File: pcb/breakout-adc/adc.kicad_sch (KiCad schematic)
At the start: 102 parts, among them J16 Conn_01x02_Pin, J17 Conn_01x02_Pin, J18 Conn_01x02_Pin, J19 Conn_01x02_Pin, U1 LMH6551MA, U2 LMH6551MA, U3 74AVC9112, U4 ADC10DL065, U5 74LS574, U6 74LS574, U7 74LS574, X1 SG-8101CE 50Mhz

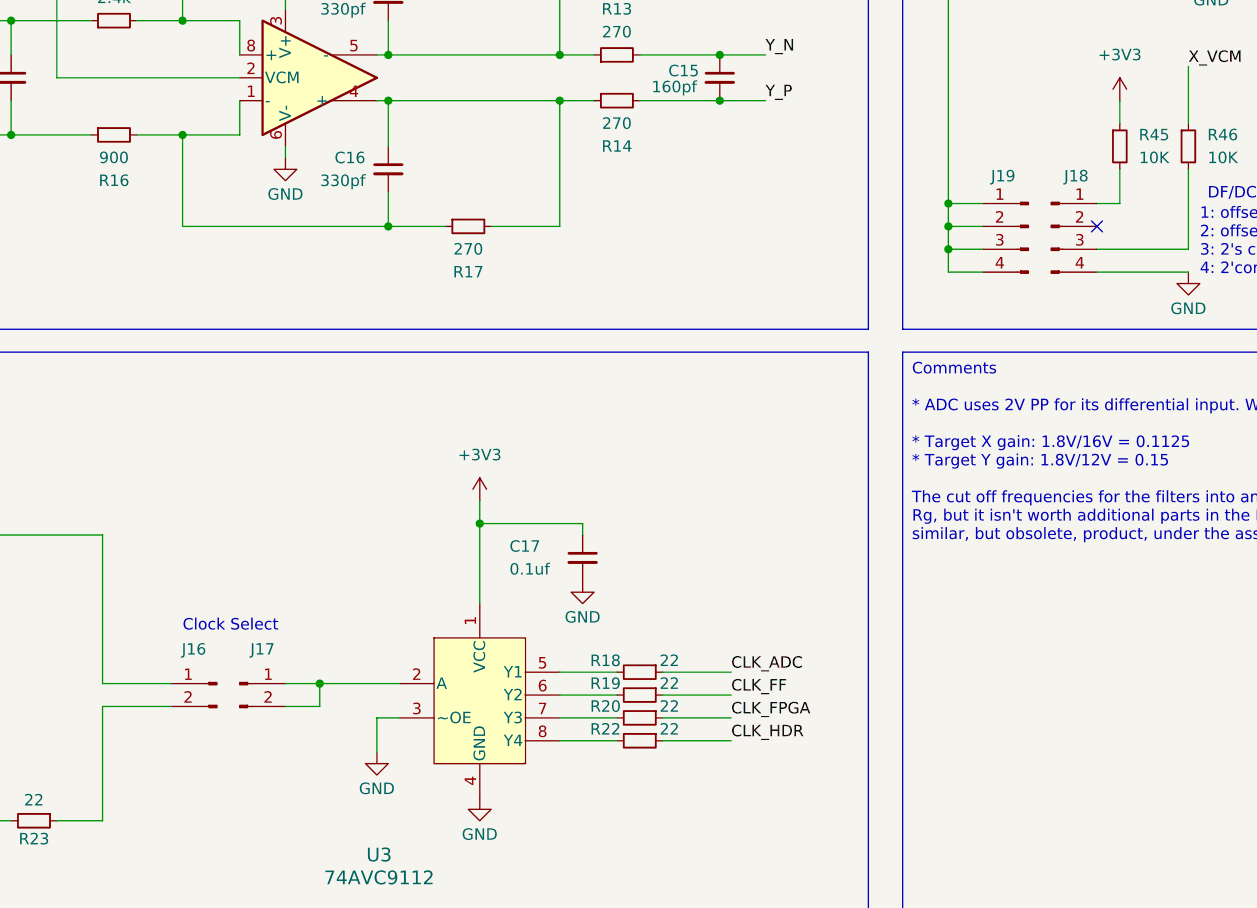
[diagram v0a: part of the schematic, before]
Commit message: [adc][pcb] assigned footprints and dropped on pcb
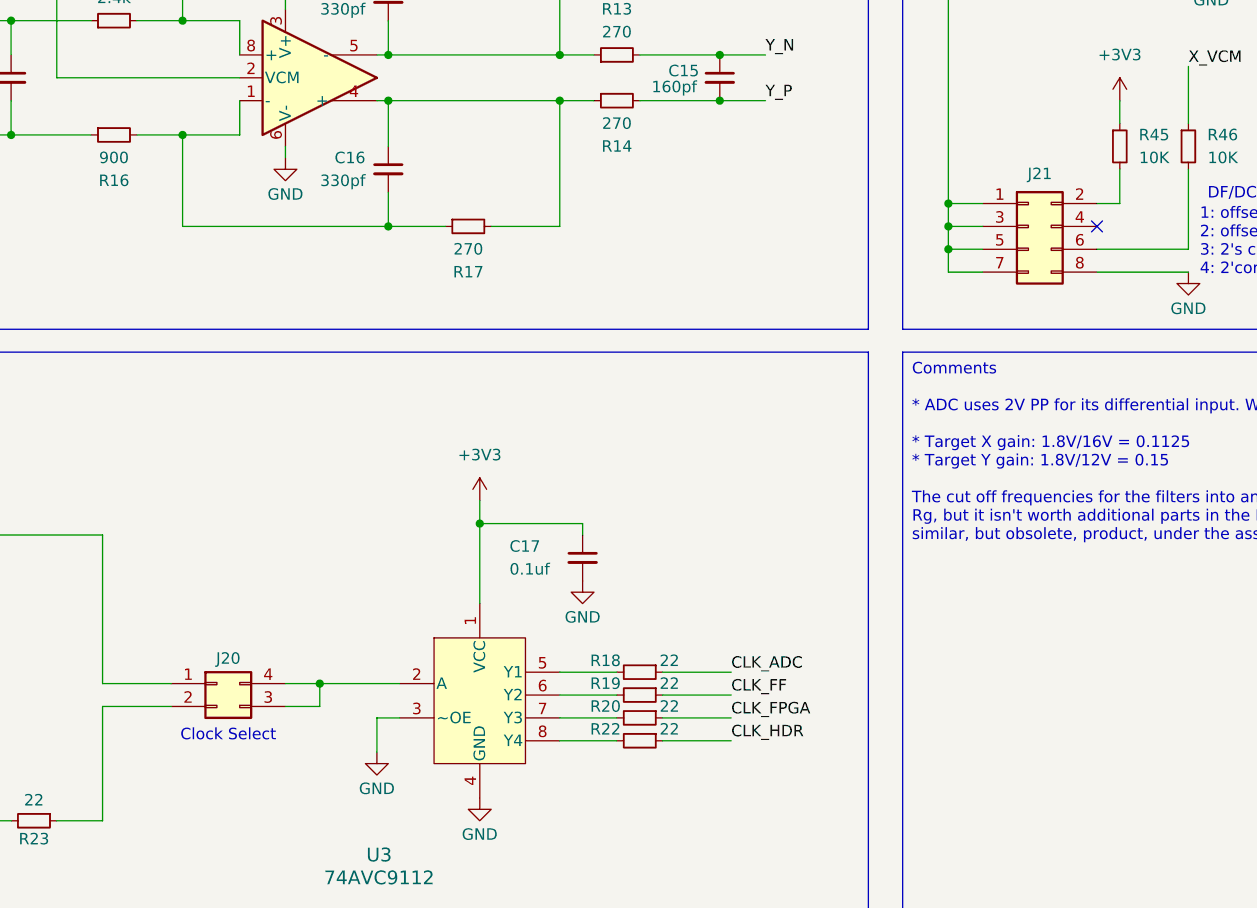
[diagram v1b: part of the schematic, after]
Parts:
- removed J16, J17: Conn_01x02_Pin, symbol Connector:Conn_01x02_Pin
- removed J18, J19: Conn_01x02_Pin, symbol Connector:Conn_01x04_Pin
- added J20: Conn_02x02_Counter_Clockwise, Connector_PinHeader_2.54mm:PinHeader_2x02_P2.54mm_Vertical, symbol Connector_Generic:Conn_02x02_Counter_Clockwise
- added J21: Conn_02x04_Odd_Even, Connector_PinHeader_2.54mm:PinHeader_2x04_P2.54mm_Vertical, symbol Connector_Generic:Conn_02x04_Odd_Even
- C13, C14, C15, C16, C5, C6, C7, C8: footprint (none) -> Capacitor_SMD:C_0402_1005Metric
- R10, R11, R12, R13, R14, R15, R16, R17, R24, R4, R45, R46, R5, R6, R7, R8, R9: footprint (none) -> Resistor_SMD:R_0603_1608Metric
- U5, U6, U7: footprint (none) -> Package_SO:TSSOP-20_4.4x6.5mm_P0.65mm; Digi-Key Part Number (none) -> 296-8532-1-ND; LCSC Part # (none) -> C7672
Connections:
- net EXT_CLK: now also J20.1 (Pin_1)
- net GND: now also J21.8 (Pin_8)
- net at U3.2 (A): now also J20.3 (Pin_3), J20.4 (Pin_4)
- net at R45.2: now also J21.2 (Pin_2)
- net at R46.2: now also J21.6 (Pin_6)
- net at U4.21 (DF/DCS): now also J21.1 (Pin_1), J21.3 (Pin_3), J21.5 (Pin_5), J21.7 (Pin_7)
- net at R23.1: now also J20.2 (Pin_2)

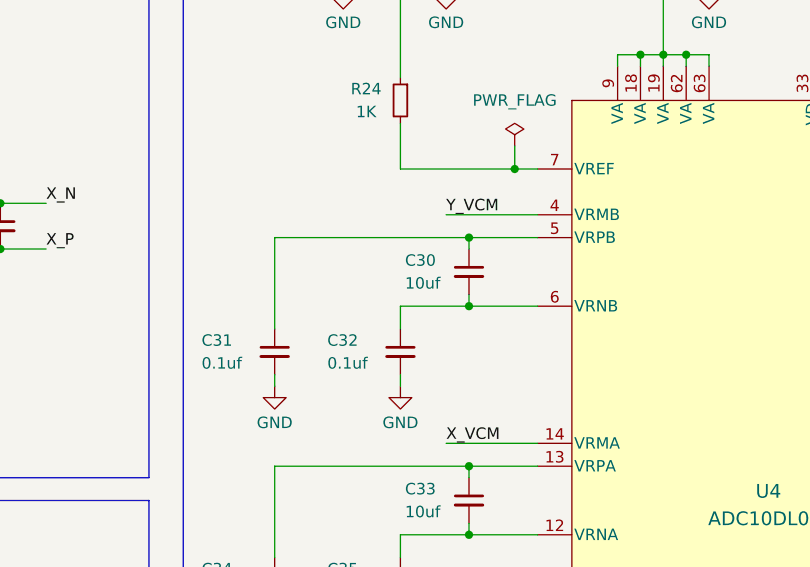
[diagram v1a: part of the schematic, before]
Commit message: [adc][pcb] initial layout of X input op amp
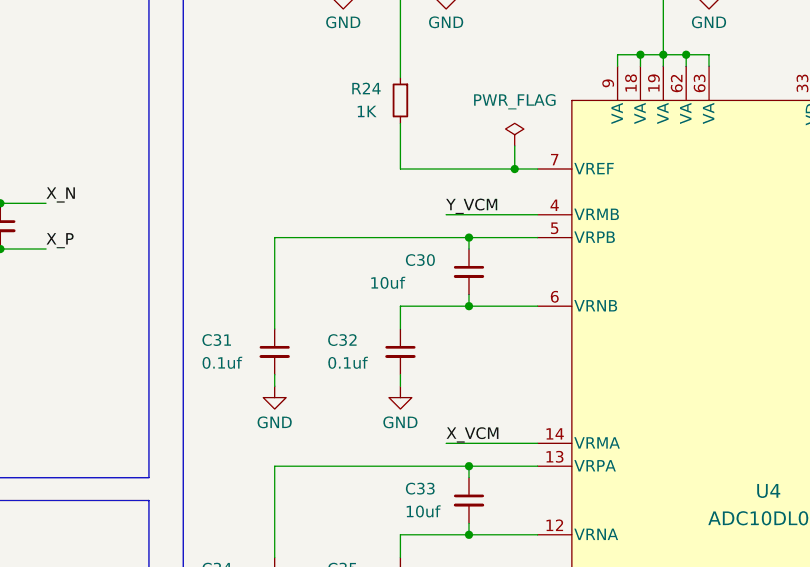
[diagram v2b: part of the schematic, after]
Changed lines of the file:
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@@
 					(size 1.27 1.27)
 				)
-				(justify left)
+				(justify right)
 			)
 		)

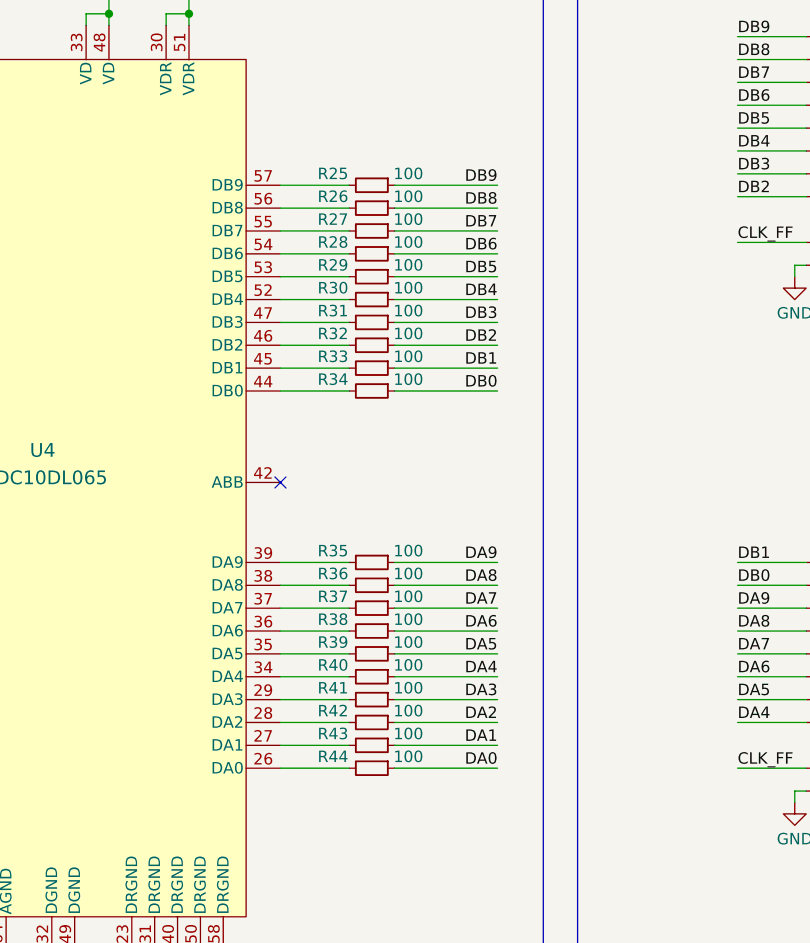
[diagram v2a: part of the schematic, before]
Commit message: [adc][pcb] switch to R arrays and place buffers
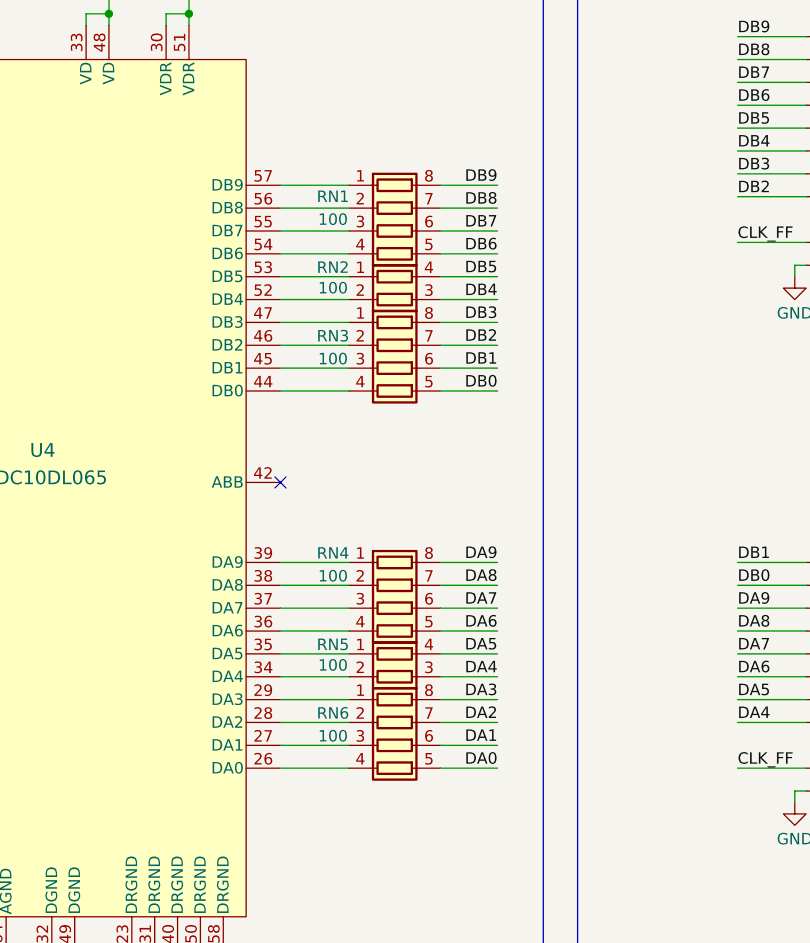
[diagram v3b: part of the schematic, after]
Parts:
- removed R25, R26, R27, R28, R29, R30, R31, R32, R33, R34, R35, R36, R37, R38, R39, R40, R41, R42, R43, R44: 100, Resistor_SMD:R_0603_1608Metric, symbol Device:R_Small
- added RN1, RN3, RN4, RN6: 100, Resistor_SMD:R_Array_Concave_4x0402, symbol Device:R_Pack04
- added RN2, RN5: 100, Resistor_SMD:R_Array_Convex_2x0402, symbol Device:R_Pack02
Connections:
- net DA0: now also RN6.5 (R4.2)
- net DA1: now also RN6.6 (R3.2)
- net DA2: now also RN6.7 (R2.2)
- net DA3: now also RN6.8 (R1.2)
- net DA4: now also RN5.3 (R2.2)
- net DA5: now also RN5.4 (R1.2)
- net DA6: now also RN4.5 (R4.2)
- net DA7: now also RN4.6 (R3.2)
- net DA8: now also RN4.7 (R2.2)
- net DA9: now also RN4.8 (R1.2)
- net DB0: now also RN3.5 (R4.2)
- net DB1: now also RN3.6 (R3.2)
- net DB2: now also RN3.7 (R2.2)
- net DB3: now also RN3.8 (R1.2)
- net DB4: now also RN2.3 (R2.2)
- net DB5: now also RN2.4 (R1.2)
- net DB6: now also RN1.5 (R4.2)
- net DB7: now also RN1.6 (R3.2)
- net DB8: now also RN1.7 (R2.2)
- net DB9: now also RN1.8 (R1.2)
- net at U4.26 (DA0): now also RN6.4 (R4.1)
- net at U4.27 (DA1): now also RN6.3 (R3.1)
- net at U4.28 (DA2): now also RN6.2 (R2.1)
- net at U4.29 (DA3): now also RN6.1 (R1.1)
- net at U4.34 (DA4): now also RN5.2 (R2.1)
- net at U4.35 (DA5): now also RN5.1 (R1.1)
- net at U4.36 (DA6): now also RN4.4 (R4.1)
- net at U4.37 (DA7): now also RN4.3 (R3.1)
- net at U4.38 (DA8): now also RN4.2 (R2.1)
- net at U4.39 (DA9): now also RN4.1 (R1.1)
- net at U4.44 (DB0): now also RN3.4 (R4.1)
- net at U4.45 (DB1): now also RN3.3 (R3.1)
- net at U4.46 (DB2): now also RN3.2 (R2.1)
- net at U4.47 (DB3): now also RN3.1 (R1.1)
- net at U4.52 (DB4): now also RN2.2 (R2.1)
- net at U4.53 (DB5): now also RN2.1 (R1.1)
- net at U4.54 (DB6): now also RN1.4 (R4.1)
- net at U4.55 (DB7): now also RN1.3 (R3.1)
- net at U4.56 (DB8): now also RN1.2 (R2.1)
- net at U4.57 (DB9): now also RN1.1 (R1.1)

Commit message: [adc][pcb] adc power caps placed and routed
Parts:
- added V8: 3.3V, symbol Simulation_SPICE:VDC
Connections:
- net +3V3: now also C27.1, C28.1, FB1.2, U4.30 (VDR), U4.51 (VDR); no longer C10.1, C11.1, C12.1, C19.1, C2.1, C20.1, C21.1, C22.1, C23.1, C24.1, C25.1, C26.1, C29.1, C3.1, C4.1, FB1.1, R24.1, U1.3 (V+), U2.3 (V+), U4.18 (VA), U4.19 (VA), U4.33 (VD), U4.48 (VD), U4.62 (VA), U4.63 (VA), U4.9 (VA)
- net GND: now also V8.2
- new net +3V3ADC: C10.1, C11.1, C12.1, C19.1, C2.1, C20.1, C21.1, C22.1, C23.1, C24.1, C25.1, C26.1, C29.1, C3.1, C4.1, FB1.1, R24.1, U1.3 (V+), U2.3 (V+), U4.18 (VA), U4.19 (VA), U4.33 (VD), U4.48 (VD), U4.62 (VA), U4.63 (VA), U4.9 (VA), V8.1
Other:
- moved on the sheet: V1

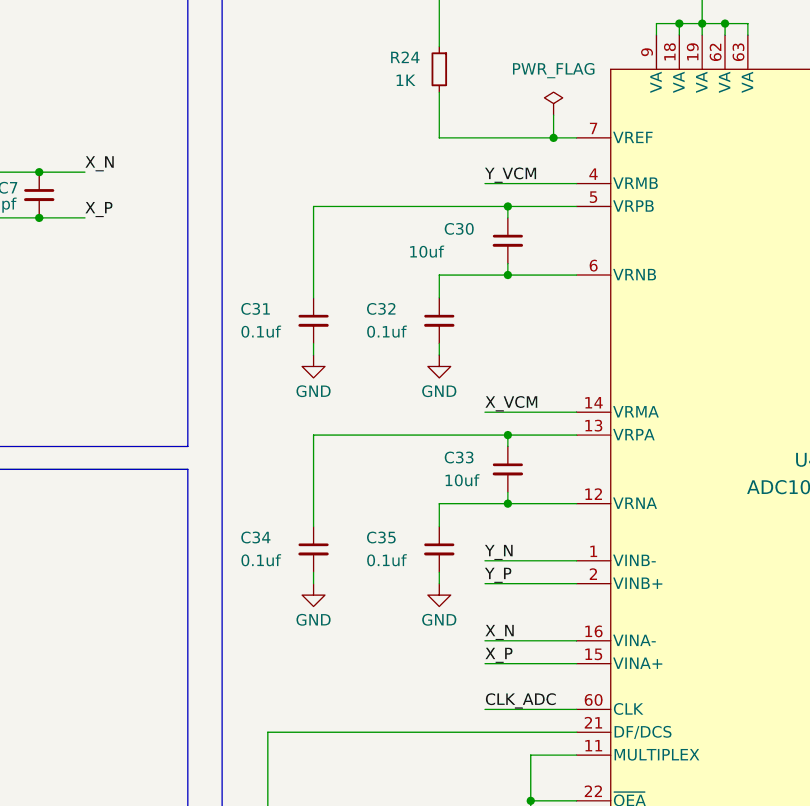
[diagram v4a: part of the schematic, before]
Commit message: [adc][pcb] passives around adc placed and routed
Had to slightly redo the power passives to squeeze in
the passives for the reference pins. Digital out
arrays moved out of the way and need to be redone.
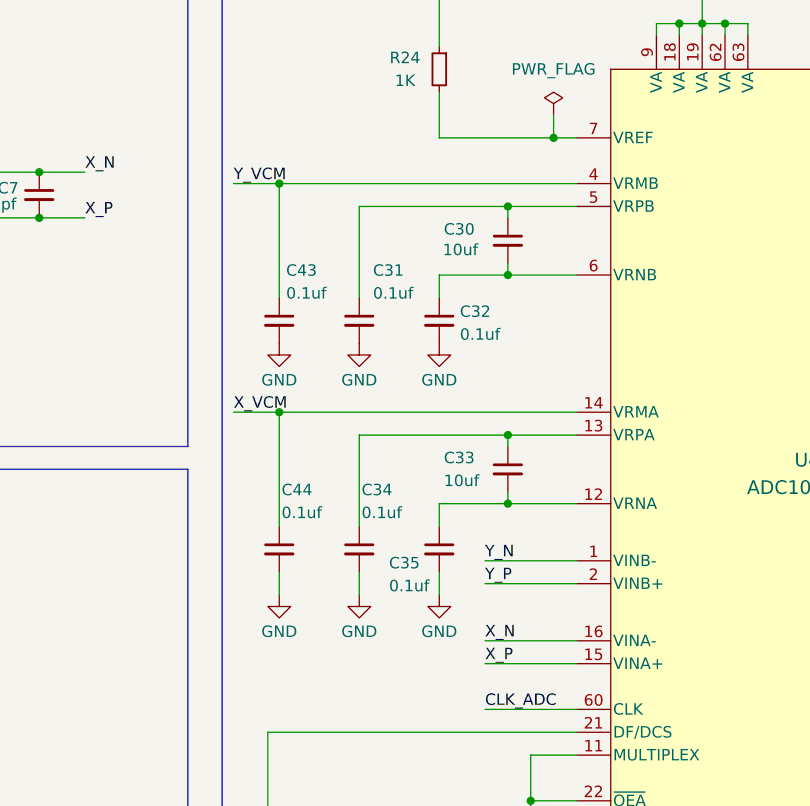
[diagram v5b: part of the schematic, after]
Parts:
- added C43, C44: 0.1uf, Capacitor_SMD:C_0402_1005Metric, symbol Device:C_Small
- R24: footprint Resistor_SMD:R_0603_1608Metric -> Resistor_SMD:R_0402_1005Metric
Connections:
- net GND: now also C43.2, C44.2
- net X_VCM: now also C44.1
- net Y_VCM: now also C43.1
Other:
- moved on the sheet: C31, C34
